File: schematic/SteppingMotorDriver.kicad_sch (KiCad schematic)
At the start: 0 parts

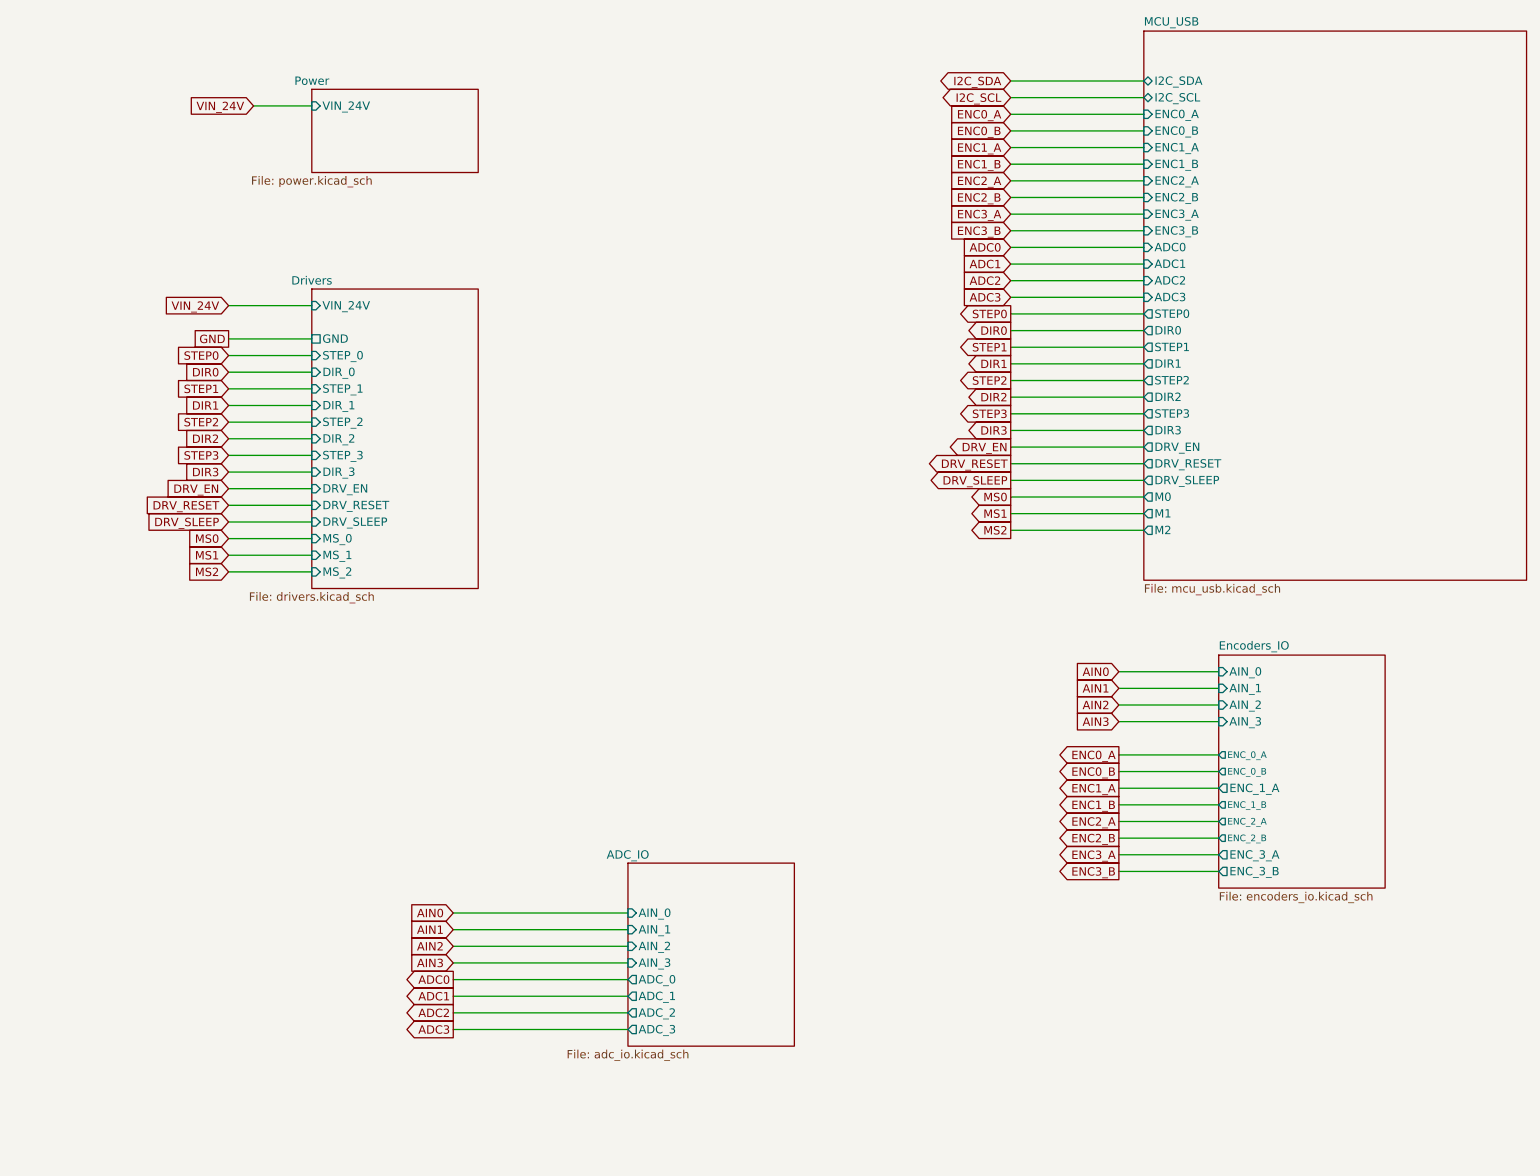
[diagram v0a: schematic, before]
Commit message: Redesign schematic to 3ch: DRV8825x3, AM26LV32 differential encoder, swap ADC3/ADC4
- DRV8825 stepper driver: 4ch -> 3ch (STEP/DIR CH0-2 on GPIO6-11)
- Encoder: 3ch differential input via AM26LV32IDR for Stepperonline 17HS15-1504-ME1K (1000PPR)
  - A+/A-, B+/B-, Z+/Z- differential pairs, GPIO15-17/18/21/35/36-37/40
- ADC assignment swap: GPIO4=MOT_V(ADC3) voltage monitor, GPIO5=CURRENT(ADC4) 100mOhm+20x amp
- Updated Gerber files (Gerber202960613 replaces Gerber202960504)
- Added AM26LV32IDR and AM26C32INSR library files
- Updated REQUIREMENTS.md: 3ch axis range, encoder specs, ADC channel table, current conversion formula
- Updated CLAUDE.md: corrected GPIO4/5 signal assignments and startup sequence

Co-Authored-By: Claude Sonnet 4.6 <noreply@anthropic.com>
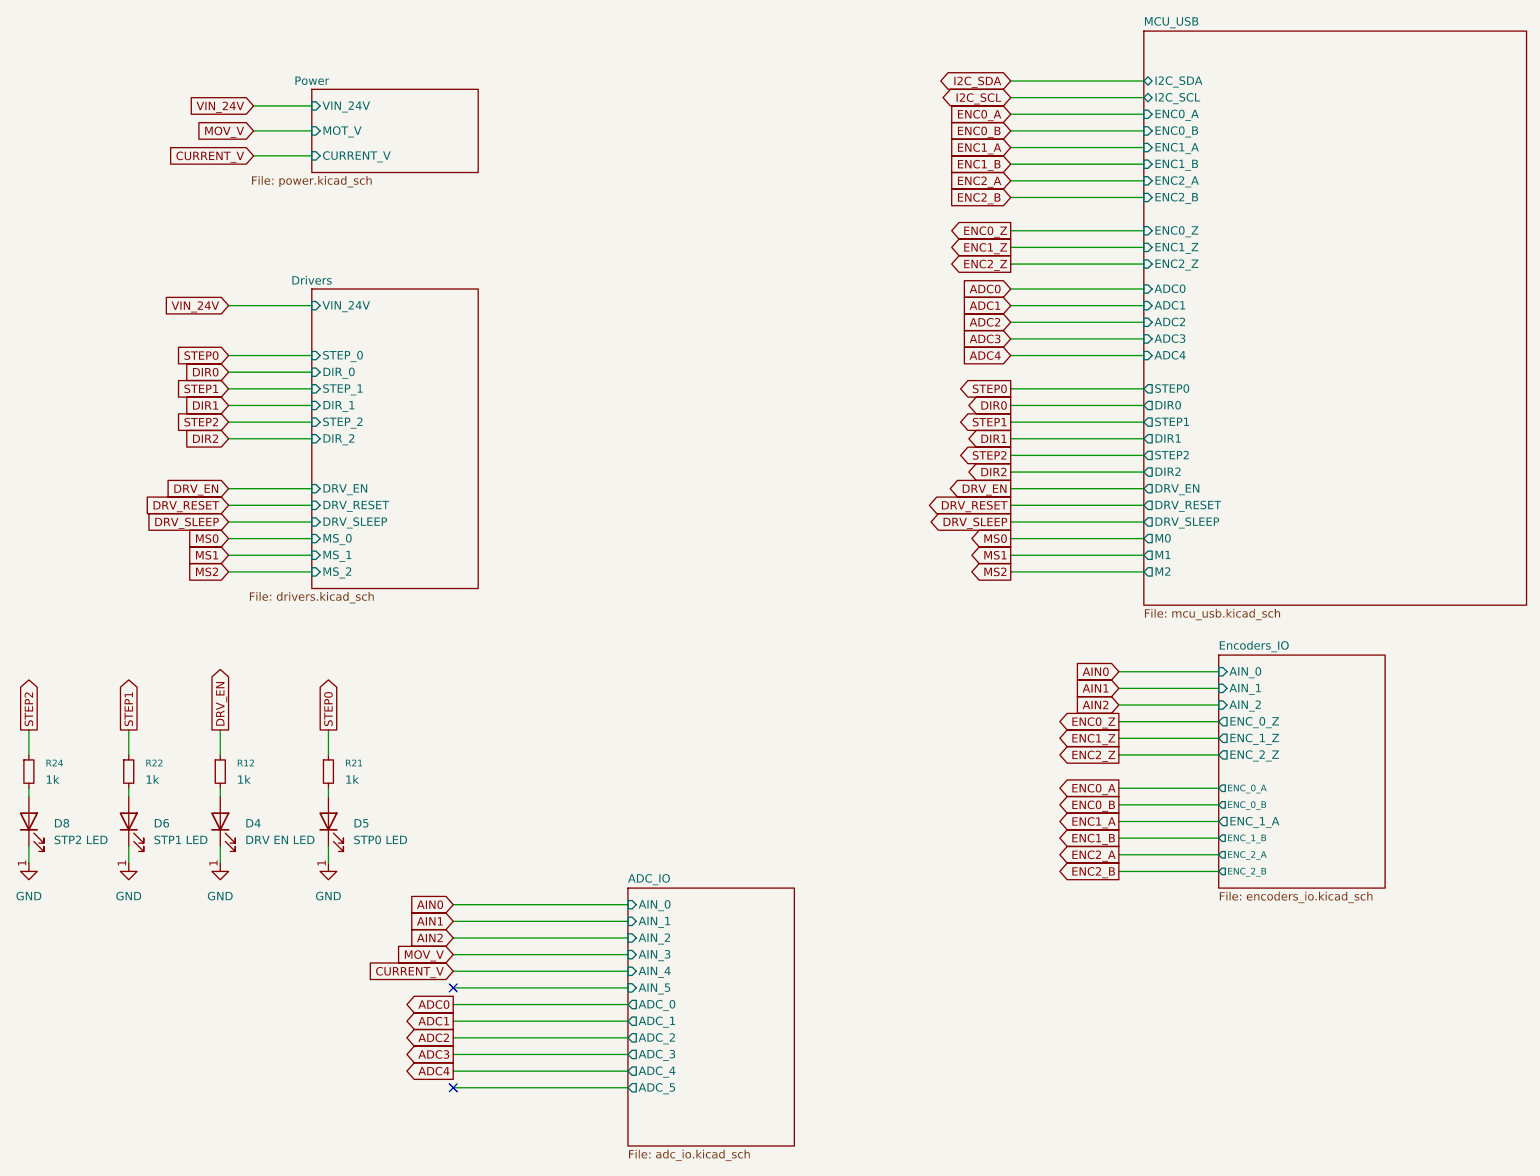
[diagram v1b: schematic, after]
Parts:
- added D4: DRV EN LED, LED_SMD:LED_0603_1608Metric, symbol Device:LED
- added D5: STP0 LED, LED_SMD:LED_0603_1608Metric, symbol Device:LED
- added D6: STP1 LED, LED_SMD:LED_0603_1608Metric, symbol Device:LED
- added D8: STP2 LED, LED_SMD:LED_0603_1608Metric, symbol Device:LED
- added R12, R21, R22, R24: 1k, Resistor_SMD:R_0603_1608Metric, symbol Device:R_Small
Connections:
- net DRV_EN: now also R12.1
- net GND: now also D4.1 (K), D5.1 (K), D6.1 (K), D8.1 (K)
- net STEP0: now also R21.1
- net STEP1: now also R22.1
- net STEP2: now also R24.1
- new net: D8.2 (A), R24.2
- new net: D5.2 (A), R21.2
- new net: D4.2 (A), R12.2
- new net: D6.2 (A), R22.2
- no-connect marks 0 -> 2
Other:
- sheet ADC_IO ports: added ADC_4, ADC_5, AIN_4, AIN_5; removed none
- sheet Drivers ports: added none; removed DIR_3, GND, STEP_3
- sheet Encoders_IO ports: added ENC_0_Z, ENC_1_Z, ENC_2_Z; removed AIN_3, ENC_3_A, ENC_3_B
- sheet MCU_USB ports: added ADC4, ENC0_Z, ENC1_Z, ENC2_Z; removed DIR3, ENC3_A, ENC3_B, STEP3
- sheet Power ports: added CURRENT_V, MOT_V; removed none
- title: (none) -> Stepping Motor Driver
